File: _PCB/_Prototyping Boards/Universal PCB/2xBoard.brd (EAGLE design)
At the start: 70 x 99 mm, 4 parts

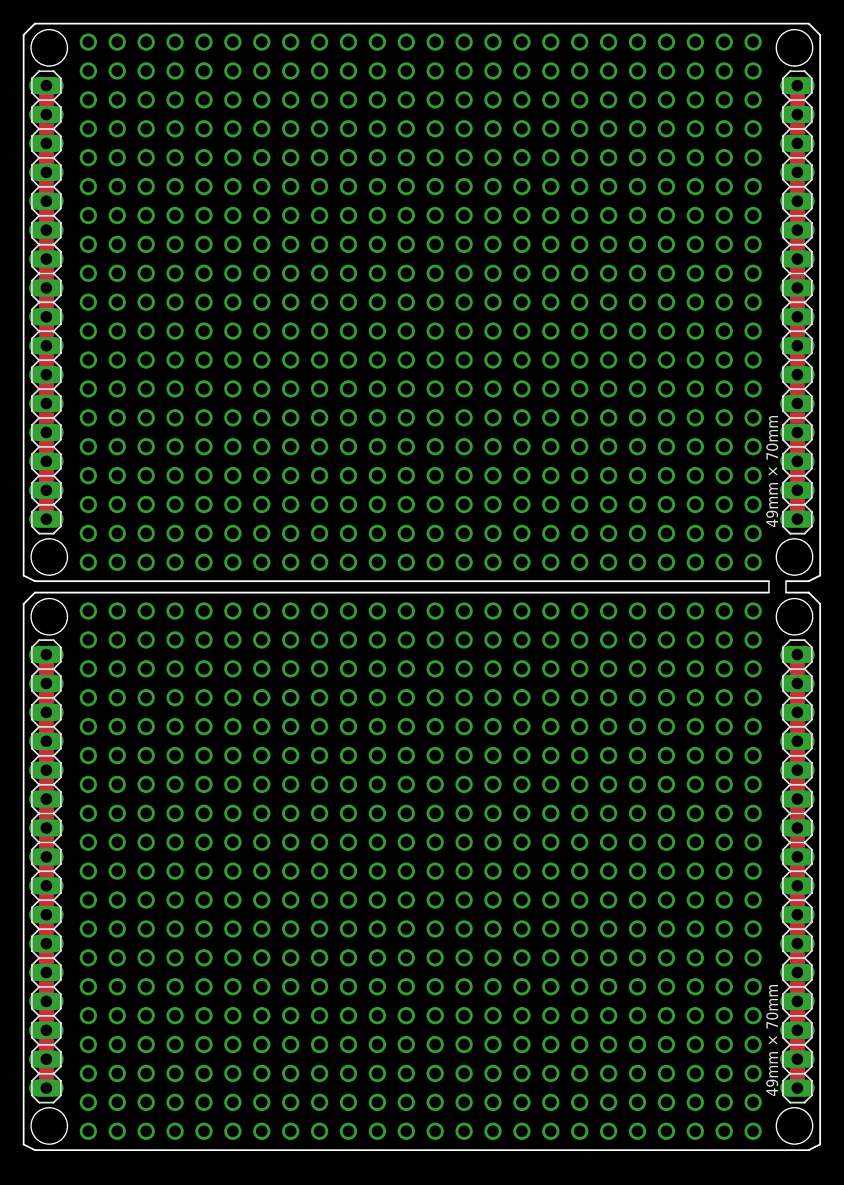
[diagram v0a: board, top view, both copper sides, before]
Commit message: CUART converter
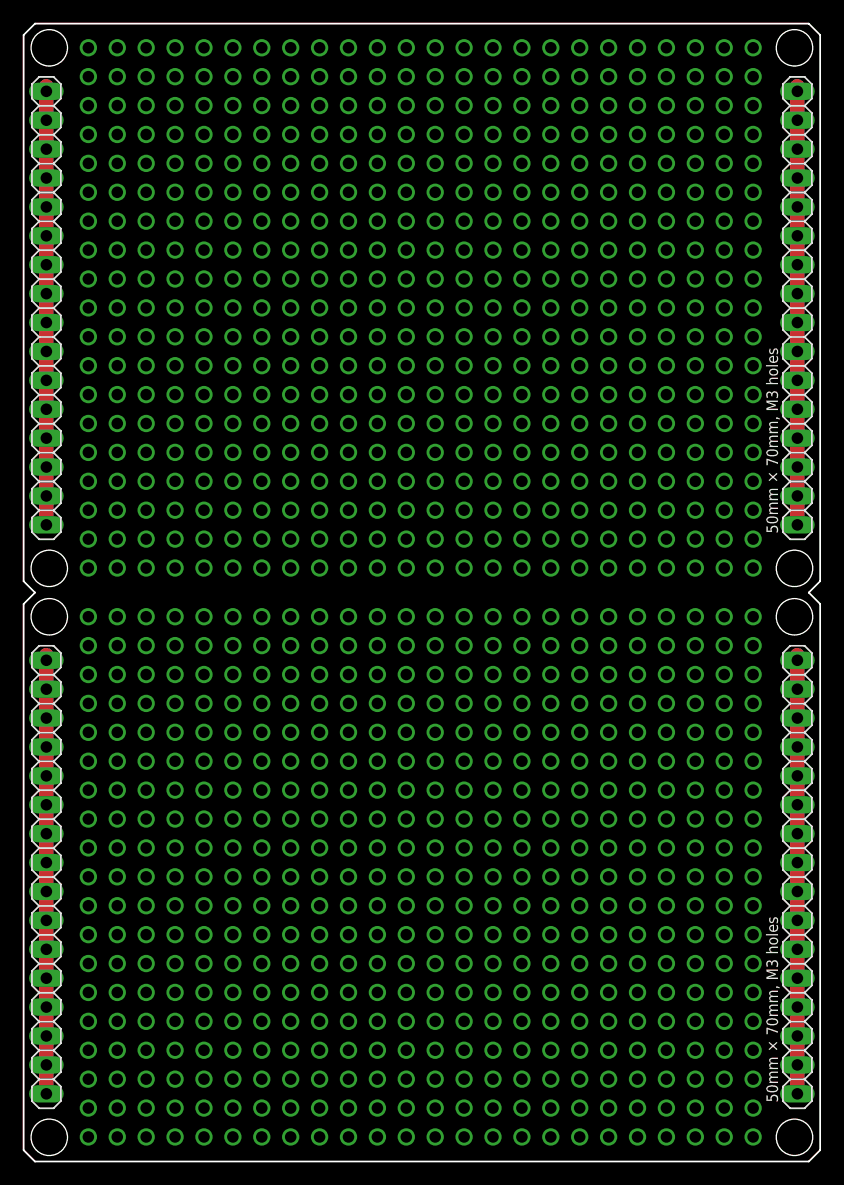
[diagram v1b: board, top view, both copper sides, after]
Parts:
- moved JP1 0.50 mm to (68.0, -26.0)
- moved JP2 0.50 mm to (2.00, -26.0)
- moved JP3 0.50 mm to (68.0, 24.0)
- moved JP4 0.50 mm to (2.00, 24.0)
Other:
- board size 70 x 99 mm -> 70 x 100 mm
- board text added: "50mm × 70mm, M3 holes"
- board text removed: "49mm × 70mm"
